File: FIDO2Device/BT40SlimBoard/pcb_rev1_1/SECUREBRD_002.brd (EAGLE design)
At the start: 30 x 30 mm, 31 parts, among them CN1 USB4105-GF-A, CN2 IF_5PIN_H, CN3 IF_2PIN_SOL, SW1 SKRPACE010, SW2 SKRPACE010, SW3 SKTADAE010, U1 BT40, U2 ADP122ACPZ-3.3-R7

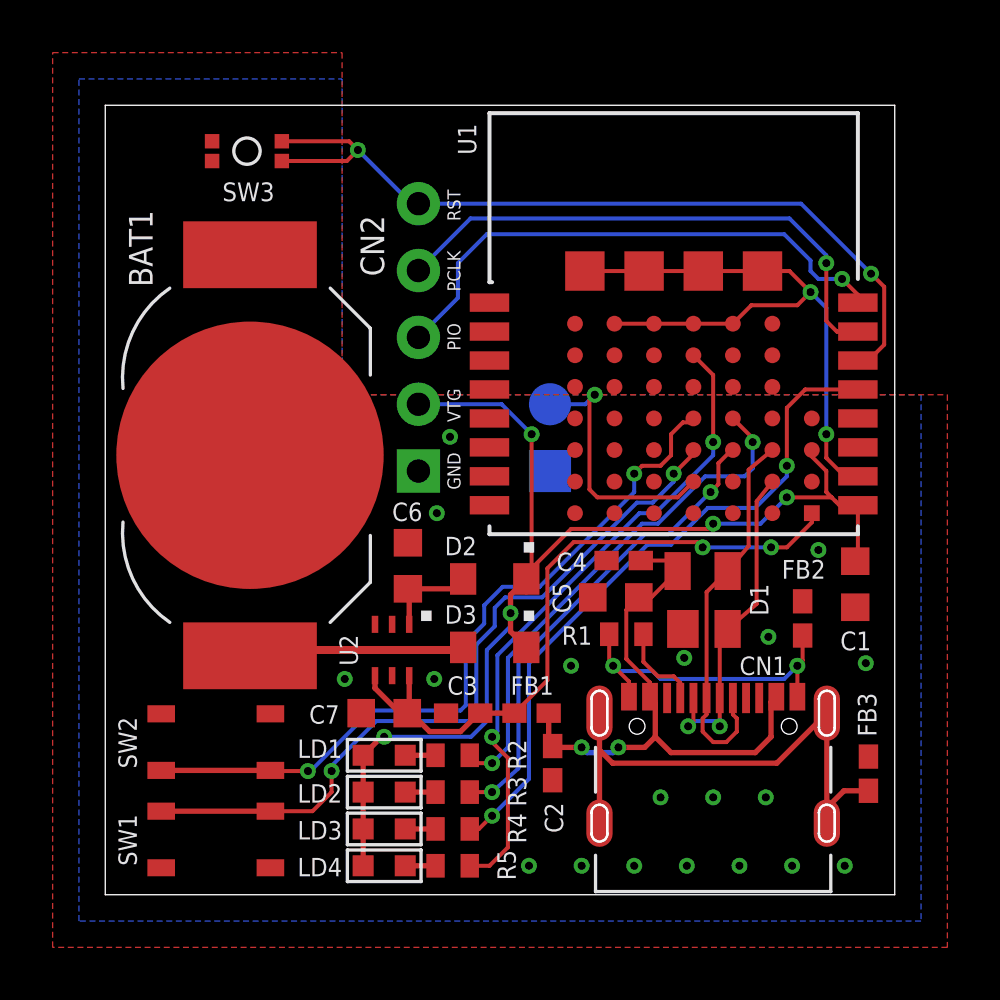
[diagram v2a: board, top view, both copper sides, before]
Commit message: 配線レイアウトを修正
・SWD／RESET周りの配線を改善
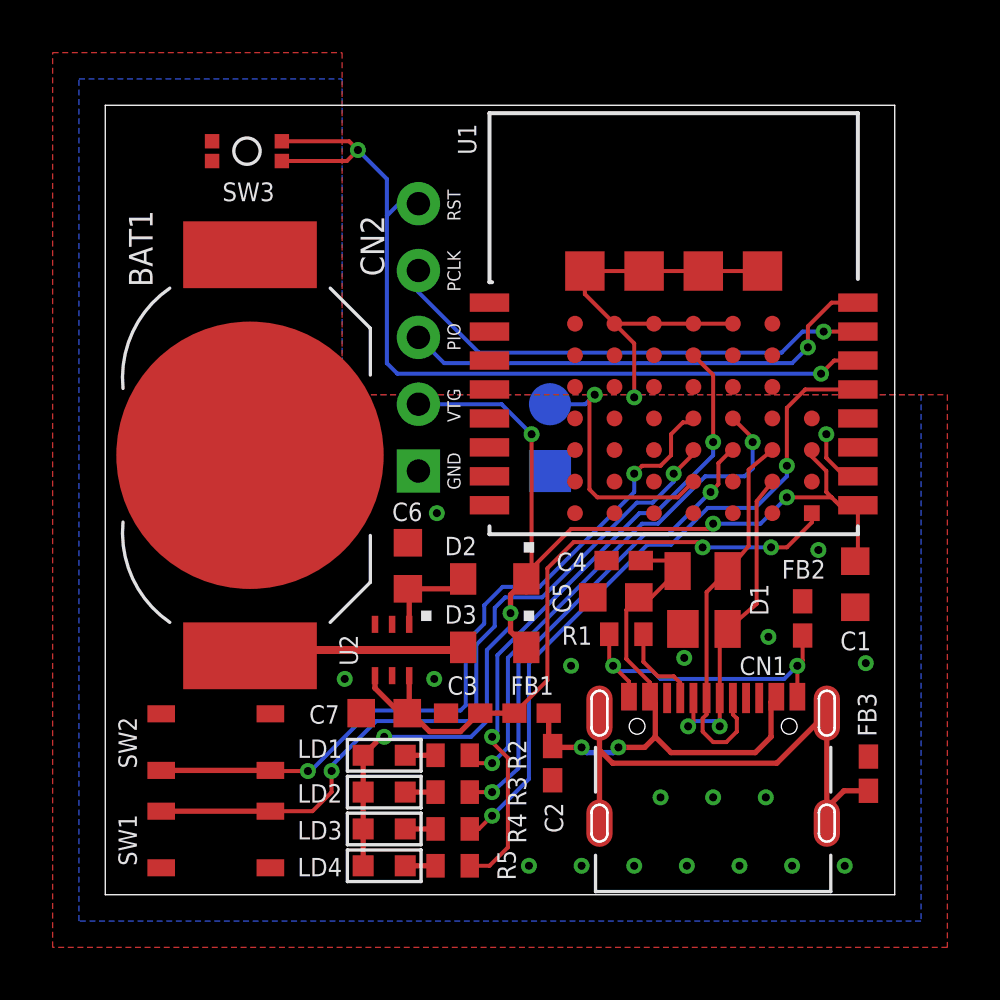
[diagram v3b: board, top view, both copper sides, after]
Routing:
- net 0V: track 24.9 -> 19.2 mm, vias 21 -> 20
- net RESET: track 31.7 -> 34.3 mm
- net SWDIO: track 20.6 -> 18.5 mm
- net SWCLK: track 20.8 -> 18.8 mm
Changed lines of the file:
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@@
 <wire x1="22.35" y1="21.7" x2="23.85" y2="21.7" width="0.1524" layer="1"/>
 <wire x1="22.35" y1="21.7" x2="20.85" y2="21.7" width="0.1524" layer="1"/>
-<wire x1="20.85" y1="21.7" x2="19.35" y2="21.7" width="0.1524" layer="1"/>
 <wire x1="18.225" y1="23.7" x2="20.475" y2="23.7" width="0.1524" layer="1"/>
 <wire x1="20.475" y1="23.7" x2="22.725" y2="23.7" width="0.1524" layer="1"/>
-<via x="26.8" y="22.9" extent="1-16" drill="0.3048"/>
-<wire x1="24.975" y1="23.7" x2="26" y2="23.7" width="0.1524" layer="1"/>
+<via x="20.1" y="18.9" extent="1-16" drill="0.3048"/>
 <wire x1="22.725" y1="23.7" x2="24.975" y2="23.7" width="0.1524" layer="1"/>
-<wire x1="26.8" y1="22.9" x2="27.4" y2="22.3" width="0.1524" layer="16"/>
-<wire x1="27.4" y1="22.3" x2="27.4" y2="17.5" width="0.1524" layer="16"/>
-<wire x1="26" y1="23.7" x2="26.8" y2="22.9" width="0.1524" layer="1"/>
 <via x="12.5" y="8.2" extent="1-16" drill="0.3048"/>
 <via x="17.7" y="8.7" extent="1-16" drill="0.3048"/>
@@
 <via x="21.1" y="3.7" extent="1-16" drill="0.3048"/>
 <via x="27.1" y="13.1" extent="1-16" drill="0.3048"/>
-<via x="13.1" y="17.4" extent="1-16" drill="0.3048"/>
 <via x="12.6" y="14.5" extent="1-16" drill="0.3048"/>
 <wire x1="27.4" y1="17.5" x2="27.4" y2="16.6" width="0.1524" layer="1"/>
 <wire x1="27.4" y1="16.6" x2="28.1" y2="15.9" width="0.1524" layer="1"/>
 <wire x1="28.1" y1="15.9" x2="28.6" y2="15.9" width="0.1524" layer="1"/>
-<wire x1="23.85" y1="21.7" x2="24.55" y2="22.4" width="0.1524" layer="1"/>
-<wire x1="24.55" y1="22.4" x2="26.3" y2="22.4" width="0.1524" layer="1"/>
-<wire x1="26.3" y1="22.4" x2="26.8" y2="22.9" width="0.1524" layer="1"/>
 <via x="9.1" y="8.2" extent="1-16" drill="0.3048"/>
 <contactref element="CN3" pad="1"/>
@@
 <via x="18.1" y="1.1" extent="1-16" drill="0.3048"/>
 <via x="16.1" y="1.1" extent="1-16" drill="0.3048"/>
+<wire x1="20.1" y1="18.9" x2="20.1" y2="20.95" width="0.1524" layer="1"/>
+<wire x1="20.1" y1="20.95" x2="19.35" y2="21.7" width="0.1524" layer="1"/>
+<wire x1="19.35" y1="21.7" x2="18.225" y2="22.825" width="0.1524" layer="1"/>
+<wire x1="18.225" y1="22.825" x2="18.225" y2="23.7" width="0.1524" layer="1"/>
+<wire x1="20.85" y1="21.7" x2="19.35" y2="21.7" width="0.1524" layer="1"/>
 </signal>
 <signal name="VBUS_NRF">
@@
 <contactref element="U1" pad="14"/>
 <contactref element="CN2" pad="5"/>
-<via x="29.1" y="23.6" extent="1-16" drill="0.3048"/>
-<wire x1="28.6" y1="20.3" x2="29" y2="20.3" width="0.1524" layer="1"/>
-<wire x1="29" y1="20.3" x2="29.6" y2="20.9" width="0.1524" layer="1"/>
-<wire x1="26.44" y1="26.26" x2="29.1" y2="23.6" width="0.1524" layer="16"/>
-<wire x1="29.6" y1="20.9" x2="29.6" y2="23.1" width="0.1524" layer="1"/>
-<wire x1="29.6" y1="23.1" x2="29.1" y2="23.6" width="0.1524" layer="1"/>
-<wire x1="11.9" y1="26.26" x2="26.44" y2="26.26" width="0.1524" layer="16"/>
+<via x="27.2" y="19.8" extent="1-16" drill="0.3048"/>
 <via x="9.6" y="28.3" extent="1-16" drill="0.3048"/>
 <wire x1="6.7096" y1="28.6316" x2="9.2684" y2="28.6316" width="0.1524" layer="1"/>
@@
 <wire x1="6.7096" y1="27.8816" x2="9.1816" y2="27.8816" width="0.1524" layer="1"/>
 <wire x1="9.1816" y1="27.8816" x2="9.6" y2="28.3" width="0.1524" layer="1"/>
-<wire x1="9.6" y1="28.3" x2="11.64" y2="26.26" width="0.1524" layer="16"/>
-<wire x1="11.64" y1="26.26" x2="11.9" y2="26.26" width="0.1524" layer="16"/>
+<wire x1="28.6" y1="20.3" x2="27.7" y2="20.3" width="0.1524" layer="1"/>
+<wire x1="27.7" y1="20.3" x2="27.2" y2="19.8" width="0.1524" layer="1"/>
+<wire x1="27.2" y1="19.8" x2="11.1" y2="19.8" width="0.1524" layer="16"/>
+<wire x1="11.1" y1="19.8" x2="10.7" y2="20.2" width="0.1524" layer="16"/>
+<wire x1="10.7" y1="20.2" x2="10.7" y2="25.8" width="0.1524" layer="16"/>
+<wire x1="10.7" y1="25.8" x2="10.7" y2="27.2" width="0.1524" layer="16"/>
+<wire x1="10.7" y1="27.2" x2="9.6" y2="28.3" width="0.1524" layer="16"/>
+<wire x1="11.9" y1="26.26" x2="11.16" y2="26.26" width="0.1524" layer="16"/>
+<wire x1="11.16" y1="26.26" x2="10.7" y2="25.8" width="0.1524" layer="16"/>
 </signal>
 <signal name="SWDIO">
 <contactref element="U1" pad="16"/>
 <contactref element="CN2" pad="3"/>
-<via x="28" y="23.4" extent="1-16" drill="0.3048"/>
-<wire x1="28.6" y1="22.5" x2="28.6" y2="22.8" width="0.1524" layer="1"/>
-<wire x1="28.6" y1="22.8" x2="28" y2="23.4" width="0.1524" layer="1"/>
-<wire x1="28" y1="23.4" x2="27.1" y2="23.4" width="0.1524" layer="16"/>
-<wire x1="27.1" y1="23.4" x2="26.8" y2="23.7" width="0.1524" layer="16"/>
-<wire x1="26.8" y1="23.7" x2="26.8" y2="24.1" width="0.1524" layer="16"/>
-<wire x1="26.8" y1="24.1" x2="25.8" y2="25.1" width="0.1524" layer="16"/>
-<wire x1="25.8" y1="25.1" x2="14.5" y2="25.1" width="0.1524" layer="16"/>
-<wire x1="14.5" y1="25.1" x2="13.4" y2="24" width="0.1524" layer="16"/>
-<wire x1="13.4" y1="24" x2="13.4" y2="22.68" width="0.1524" layer="16"/>
-<wire x1="11.9" y1="21.18" x2="13.4" y2="22.68" width="0.1524" layer="16"/>
+<via x="26.7" y="20.8" extent="1-16" drill="0.3048"/>
+<wire x1="26.7" y1="20.8" x2="26.1" y2="20.2" width="0.1524" layer="16"/>
+<wire x1="26.1" y1="20.2" x2="12.88" y2="20.2" width="0.1524" layer="16"/>
+<wire x1="11.9" y1="21.18" x2="12.88" y2="20.2" width="0.1524" layer="16"/>
+<wire x1="28.6" y1="22.5" x2="27.6" y2="22.5" width="0.1524" layer="1"/>
+<wire x1="27.6" y1="22.5" x2="26.7" y2="21.6" width="0.1524" layer="1"/>
+<wire x1="26.7" y1="21.6" x2="26.7" y2="20.8" width="0.1524" layer="1"/>
 </signal>
 <signal name="SWCLK">
 <contactref element="U1" pad="15"/>
 <contactref element="CN2" pad="4"/>
-<via x="27.4" y="24" extent="1-16" drill="0.3048"/>
-<wire x1="28.6" y1="21.4" x2="27.8" y2="21.4" width="0.1524" layer="1"/>
-<wire x1="27.8" y1="21.4" x2="27.4" y2="21.8" width="0.1524" layer="1"/>
-<wire x1="27.4" y1="21.8" x2="27.4" y2="24" width="0.1524" layer="1"/>
-<wire x1="27.4" y1="24" x2="27.4" y2="24.3" width="0.1524" layer="16"/>
-<wire x1="27.4" y1="24.3" x2="26" y2="25.7" width="0.1524" layer="16"/>
-<wire x1="26" y1="25.7" x2="13.88" y2="25.7" width="0.1524" layer="16"/>
-<wire x1="11.9" y1="23.72" x2="13.88" y2="25.7" width="0.1524" layer="16"/>
+<via x="27.3" y="21.4" extent="1-16" drill="0.3048"/>
+<wire x1="27.3" y1="21.4" x2="26.5" y2="21.4" width="0.1524" layer="16"/>
+<wire x1="26.5" y1="21.4" x2="25.7" y2="20.6" width="0.1524" layer="16"/>
+<wire x1="11.9" y1="23.72" x2="11.9" y2="22.9" width="0.1524" layer="16"/>
+<wire x1="25.7" y1="20.6" x2="14.2" y2="20.6" width="0.1524" layer="16"/>
+<wire x1="14.2" y1="20.6" x2="11.9" y2="22.9" width="0.1524" layer="16"/>
+<wire x1="27.3" y1="21.4" x2="28.6" y2="21.4" width="0.1524" layer="1"/>
 </signal>
 <signal name="VBUS">

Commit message: 配線レイアウトを修正
・プログラム用スルーホールと電池ケースの位置を再調整
（電池のマイナス面がVTGピンに当たる可能性を小さくするための措置）
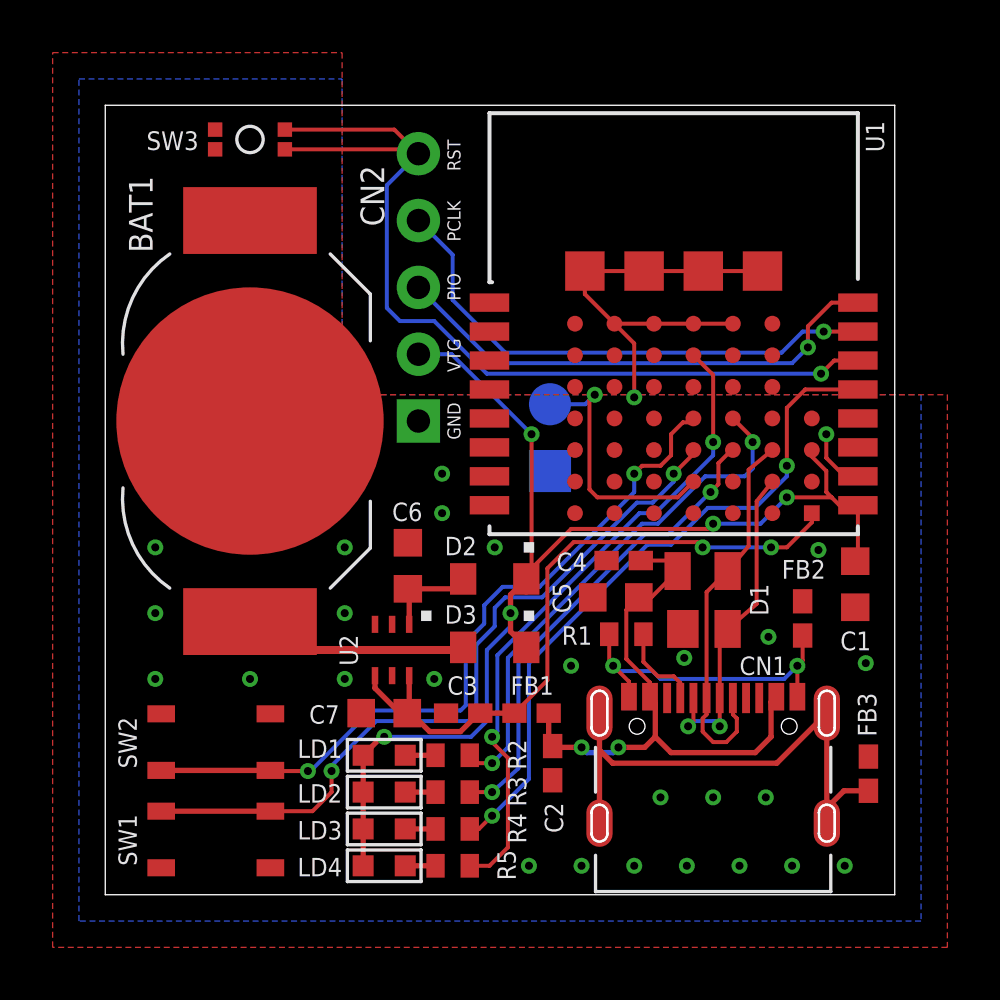
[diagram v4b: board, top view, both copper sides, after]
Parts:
- moved CN2 1.90 mm to (11.9, 18.0)
- moved BAT1 1.30 mm to (5.50, 18.0)
- moved SW3 0.46 mm to (5.50, 28.7)
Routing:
- net RESET: track 34.3 -> 36.1 mm, vias 2 -> 1
- net SWCLK: track 18.8 -> 20.1 mm
- net SWDIO: track 18.5 -> 19.3 mm
- net VDD_NRF: track 46.6 -> 47.4 mm
- net 0V: vias 20 -> 28
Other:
- board text removed: "AIN0"
- board text removed: "AIN1"

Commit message: 配線レイアウトを修正
・リアルタイムクロックモジュール配置に伴う変更
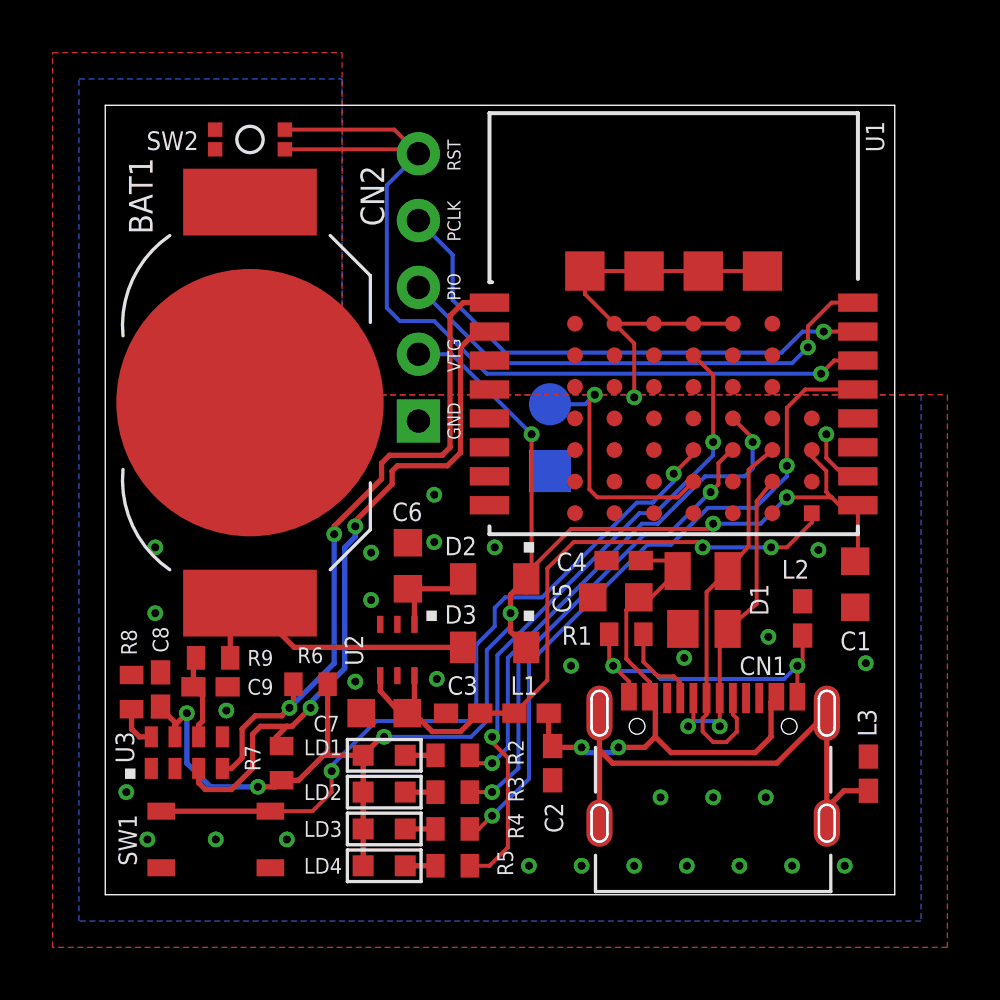
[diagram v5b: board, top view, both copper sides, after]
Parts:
- removed SW3: SKTADAE010, Parts:SKTADAE010
- added C8, C9: 0.1uF, Parts:C0402K
- added R6, R7, R8: 10k, Parts:R0402
- added R9: 390, Parts:R0402
- added U3: RV-3028-C7, ICs:SON-8
- SW2: value SKRPACE010 -> SKTADAE010; device Parts:SKRPACE010 -> Parts:SKTADAE010
- moved SW2 22.9 mm to (5.50, 28.7)
- moved BAT1 0.70 mm to (5.50, 18.7)
- moved U2 0.20 mm to (11.1, 9.30)
- renumbered FB1 to L1, FB2 to L2, FB3 to L3
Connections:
- removed net N$5: BAT1.+@2, D3.A
- removed net SW2: SW2.1, SW2.2, U1.C3
- new net N$4: R8.2, U3.8
- new net N$9: C9.1, R9.1, U3.6
- new net SCL: R7.1, U1.2, U3.3
- new net SDA: R6.1, U1.1, U3.4
- new net VDD_BAT: BAT1.+@2, D3.A, R9.2
- net 0V: now also C8.2, C9.2, R8.1, SW2.2, U3.5; no longer SW2.3, SW3.2, SW3.4
- net RESET: now also SW2.1, SW2.3; no longer SW3.1, SW3.3
- net VDD_NRF: now also C8.1, R6.2, R7.2, U3.7
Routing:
- net SW2: track 28.6 -> 0.00 mm, vias 2 -> 0
- net SCL: track 0.00 -> 26.4 mm, vias 0 -> 2
- net SDA: track 0.00 -> 25.4 mm, vias 0 -> 2
- net VDD_NRF: track 47.4 -> 61.6 mm, vias 5 -> 7
- net VDD_BAT: track 0.00 -> 11.2 mm
- net N$5: track 8.59 -> 0.00 mm
- net N$9: track 0.00 -> 3.25 mm
- net N$4: track 0.00 -> 1.62 mm
- net 0V: vias 28 -> 31
